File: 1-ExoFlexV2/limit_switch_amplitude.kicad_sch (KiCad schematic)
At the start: 44 parts, among them U21 SN74LVC3G14DCUT_V2, U22 SN74LVC3G14DCUT_V2, U23 SN74LVC3G14DCUT_V2, U24 SN74LVC3G14DCUT_V2, U25 SN74LVC3G14DCUT_V2, U26 SN74LVC3G14DCUT_V2, U27 SN74LVC3G14DCUT_V2, U28 SN74LVC1G32DBVR, U29 SN74LVC1G32DBVR

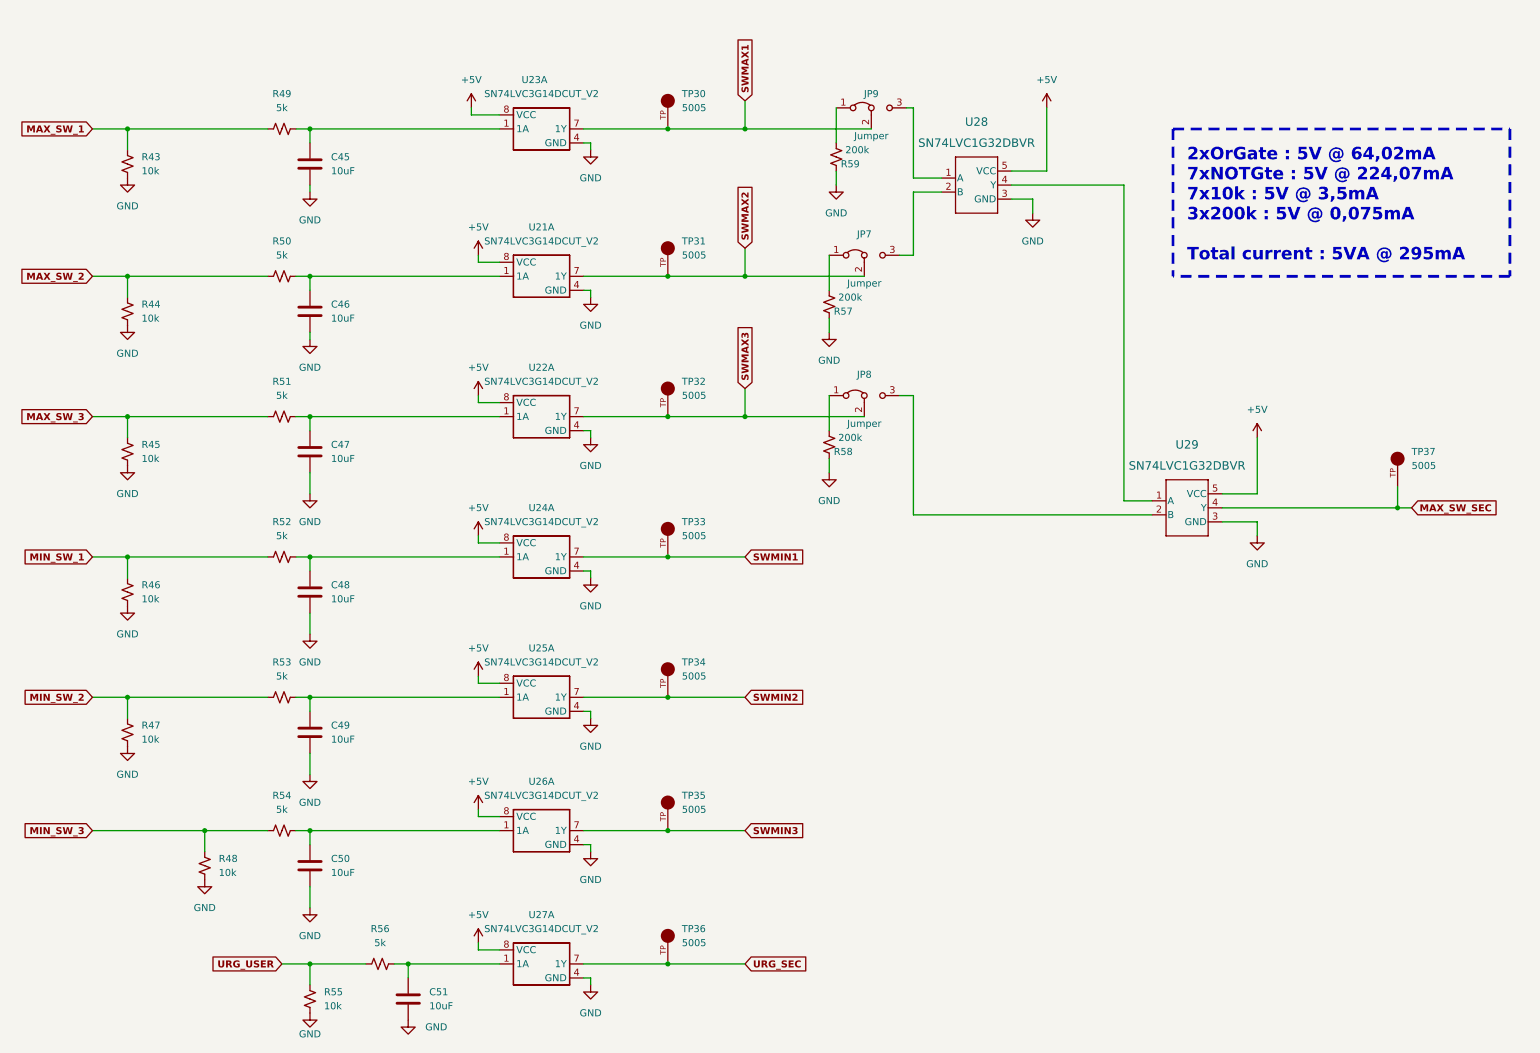
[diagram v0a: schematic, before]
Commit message: Chokes et RC
- Ajout des RF chokes
- Changement des résistance pour 0805
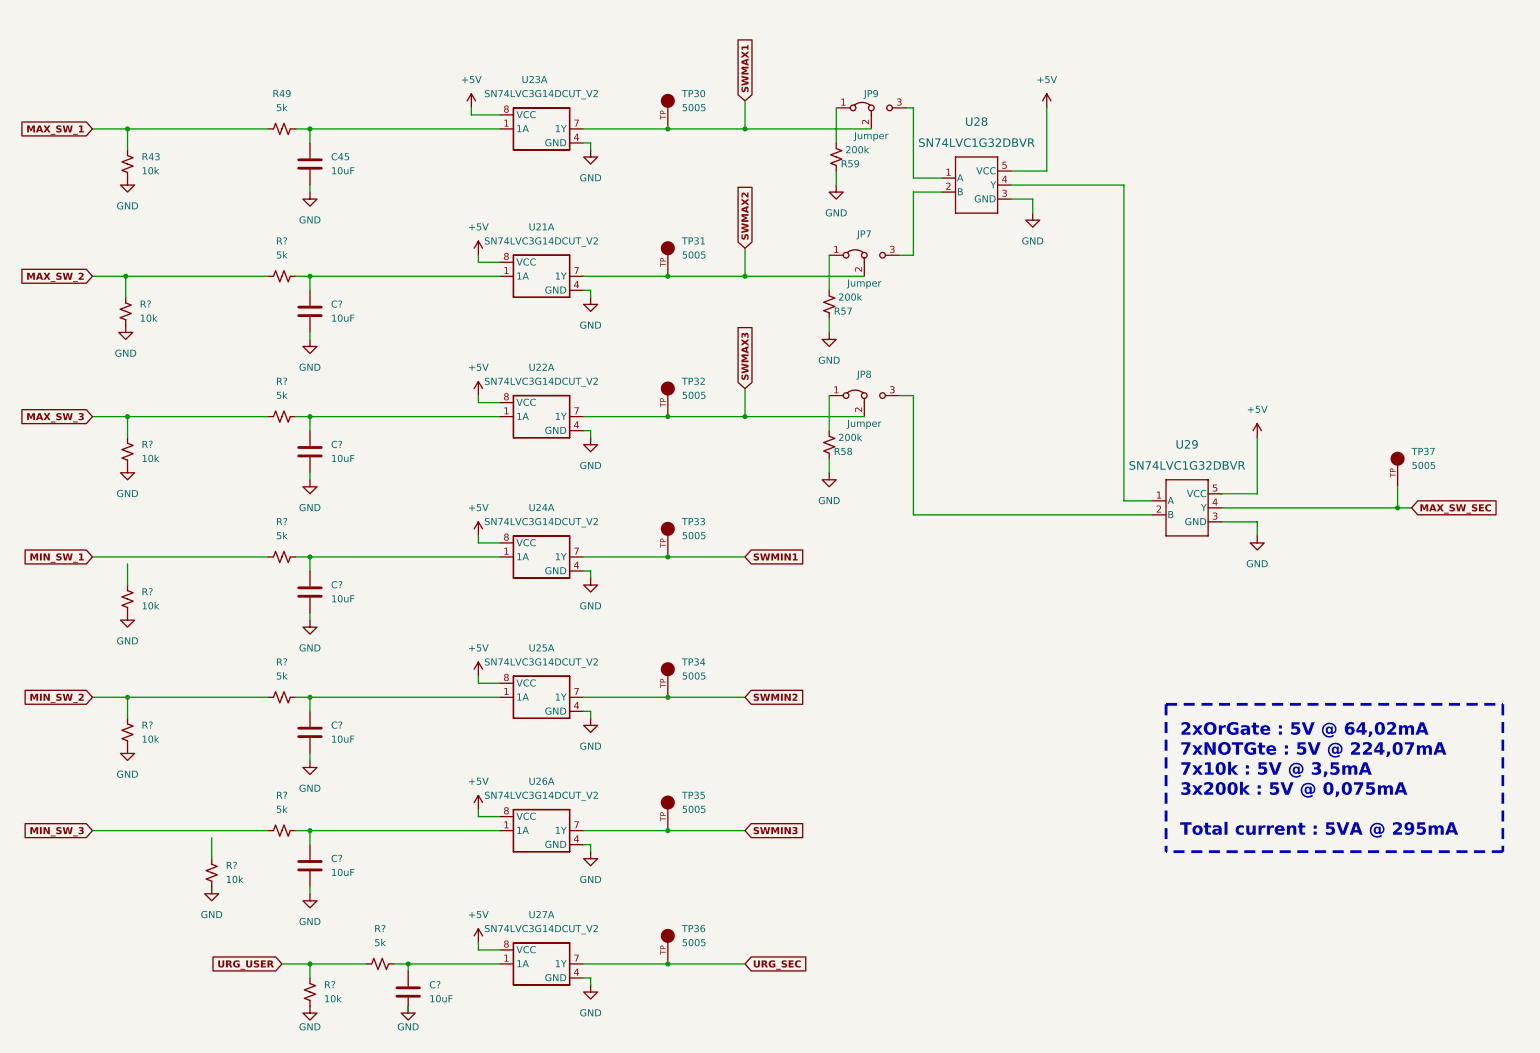
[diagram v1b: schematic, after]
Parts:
- removed C46, C47, C48, C49, C50, C51: 10uF, Capacitor_SMD:C_0603_1608Metric, symbol Device:C
- removed R44, R45, R46, R47, R48, R55: 10k, Resistor_SMD:R_0603_1608Metric, symbol Device:R_Small_US
- removed R50, R51, R52, R53, R54, R56: 5k, Resistor_SMD:R_0603_1608Metric, symbol Device:R_Small_US
- added C? (x6): 10uF, Capacitor_SMD:C_0805_2012Metric, symbol Device:C
- added R? (x6): 5k, Resistor_SMD:R_0805_2012Metric, symbol Device:R_Small_US
- added R? (x6): 10k, Resistor_SMD:R_0805_2012Metric, symbol Device:R_Small_US
- C45: footprint Capacitor_SMD:C_0603_1608Metric -> Capacitor_SMD:C_0805_2012Metric
- R43, R49: footprint Resistor_SMD:R_0603_1608Metric -> Resistor_SMD:R_0805_2012Metric
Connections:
- net GND: now also C?.2, C?.2, C?.2, C?.2, C?.2, C?.2, R?.2, R?.2, R?.2, R?.2, R?.2, R?.2
- net MAX_SW_2: now also R?.1, R?.1
- net MAX_SW_3: now also R?.1, R?.1
- net MIN_SW_1: now also R?.1
- net MIN_SW_2: now also R?.1, R?.1
- net MIN_SW_3: now also R?.1
- net URG_USER: now also R?.1, R?.1
- net at U22.1 (1A): now also C?.1, R?.2
- net at U21.1 (1A): now also C?.1, R?.2
- net at U27.1 (1A): now also C?.1, R?.2
- net at U26.1 (1A): now also C?.1, R?.2
- net at U24.1 (1A): now also C?.1, R?.2
- net at U25.1 (1A): now also C?.1, R?.2

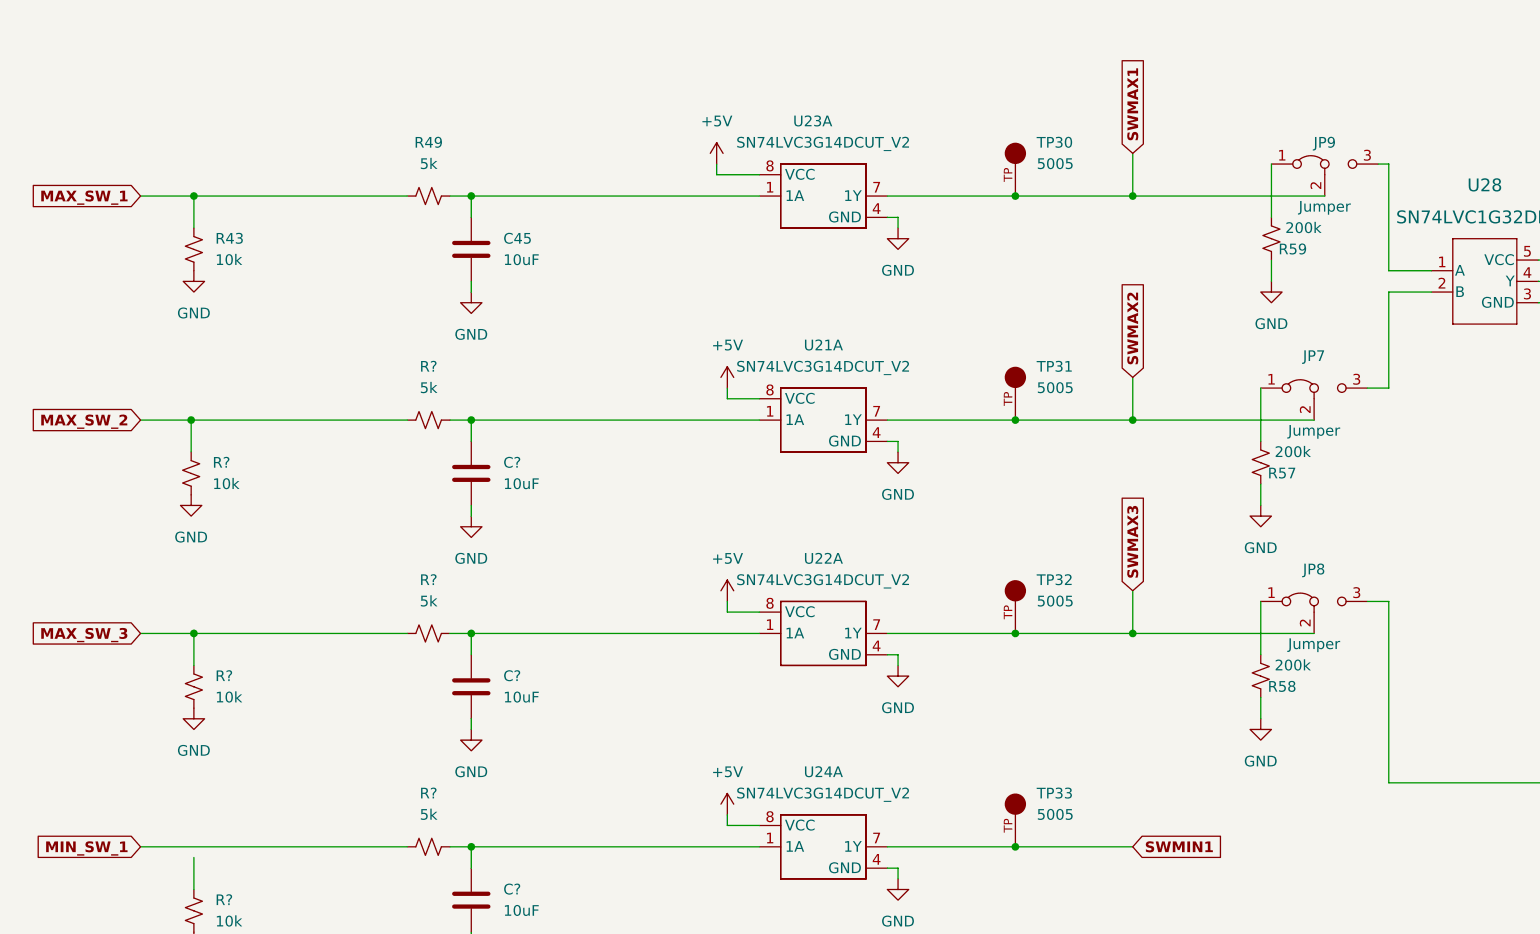
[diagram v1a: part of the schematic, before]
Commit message: Trimmer et jumper
-Changement de symbole de jumper
-Ajout des des trimmer aux endroits nécessaires
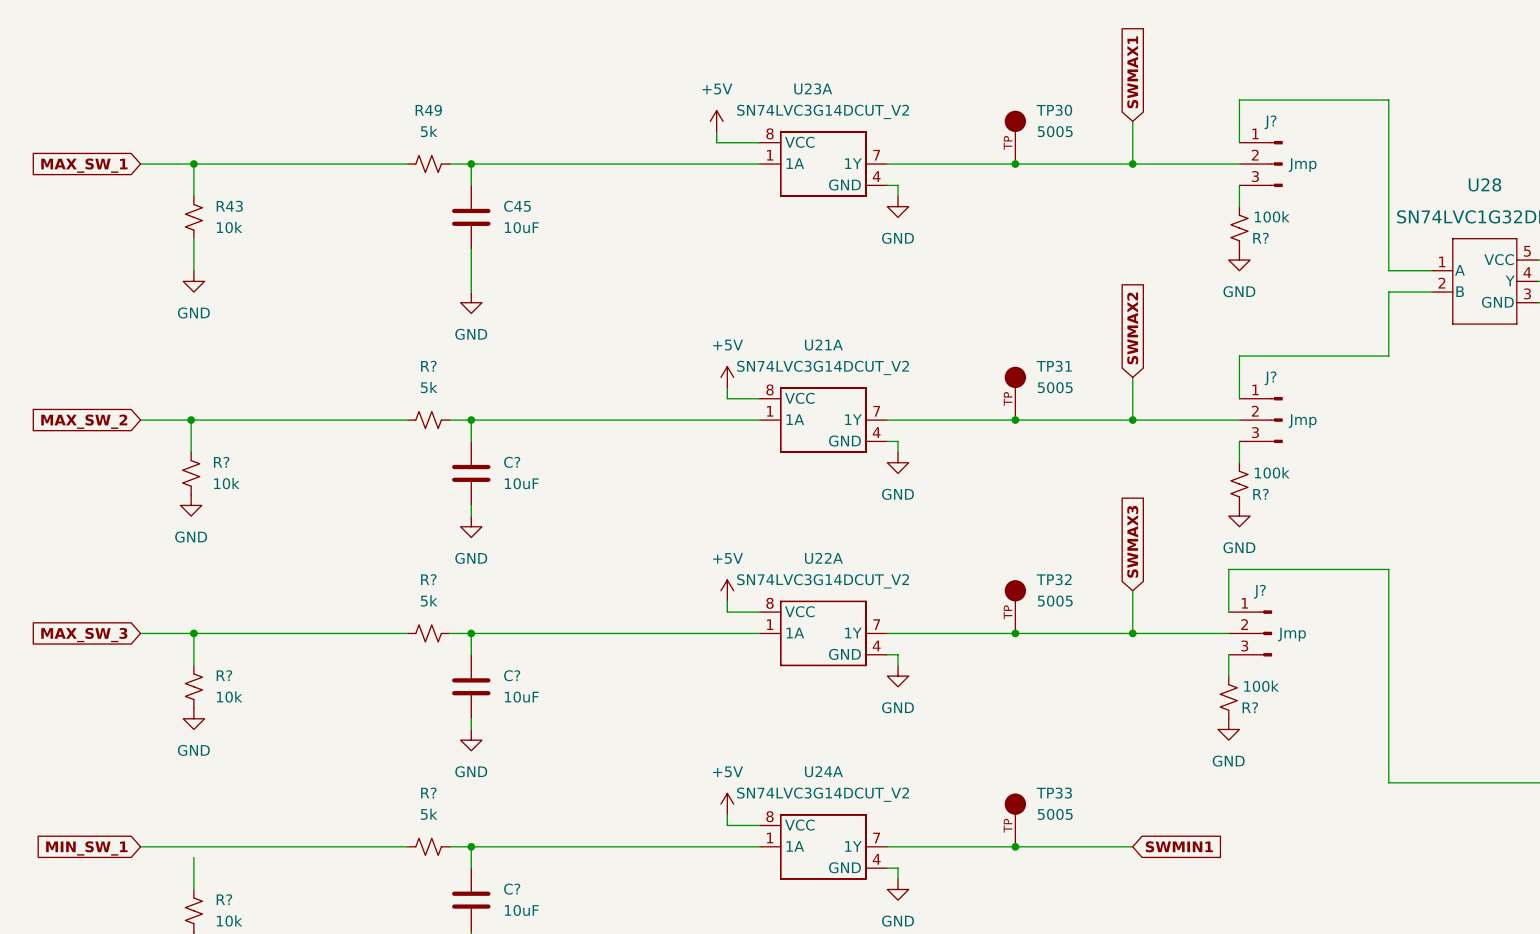
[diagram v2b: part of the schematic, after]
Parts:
- removed JP7, JP8, JP9: Jumper, Connector_PinHeader_2.54mm:PinHeader_1x03_P2.54mm_Vertical, symbol Jumper:Jumper_3_Bridged12
- removed R57, R58, R59: 200k, Resistor_SMD:R_0603_1608Metric, symbol Device:R_Small_US
- added J? (x3): Jmp, symbol Connector:Conn_01x03_Male
- added R? (x3): 100k, Resistor_SMD:R_0805_2012Metric, symbol Device:R_Small_US
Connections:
- net GND: now also R?.2, R?.2, R?.2
- net SWMAX1: now also J?.2 (Pin_2)
- net SWMAX2: now also J?.2 (Pin_2)
- net SWMAX3: now also J?.2 (Pin_2)
- net at U28.2 (B): now also J?.1 (Pin_1)
- net at U29.2 (B): now also J?.1 (Pin_1)
- net at U28.1 (A): now also J?.1 (Pin_1)
- new net: J?.3 (Pin_3), R?.1 (x3)
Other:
- moved on the sheet: C45, R43, R49, TP30, U23A

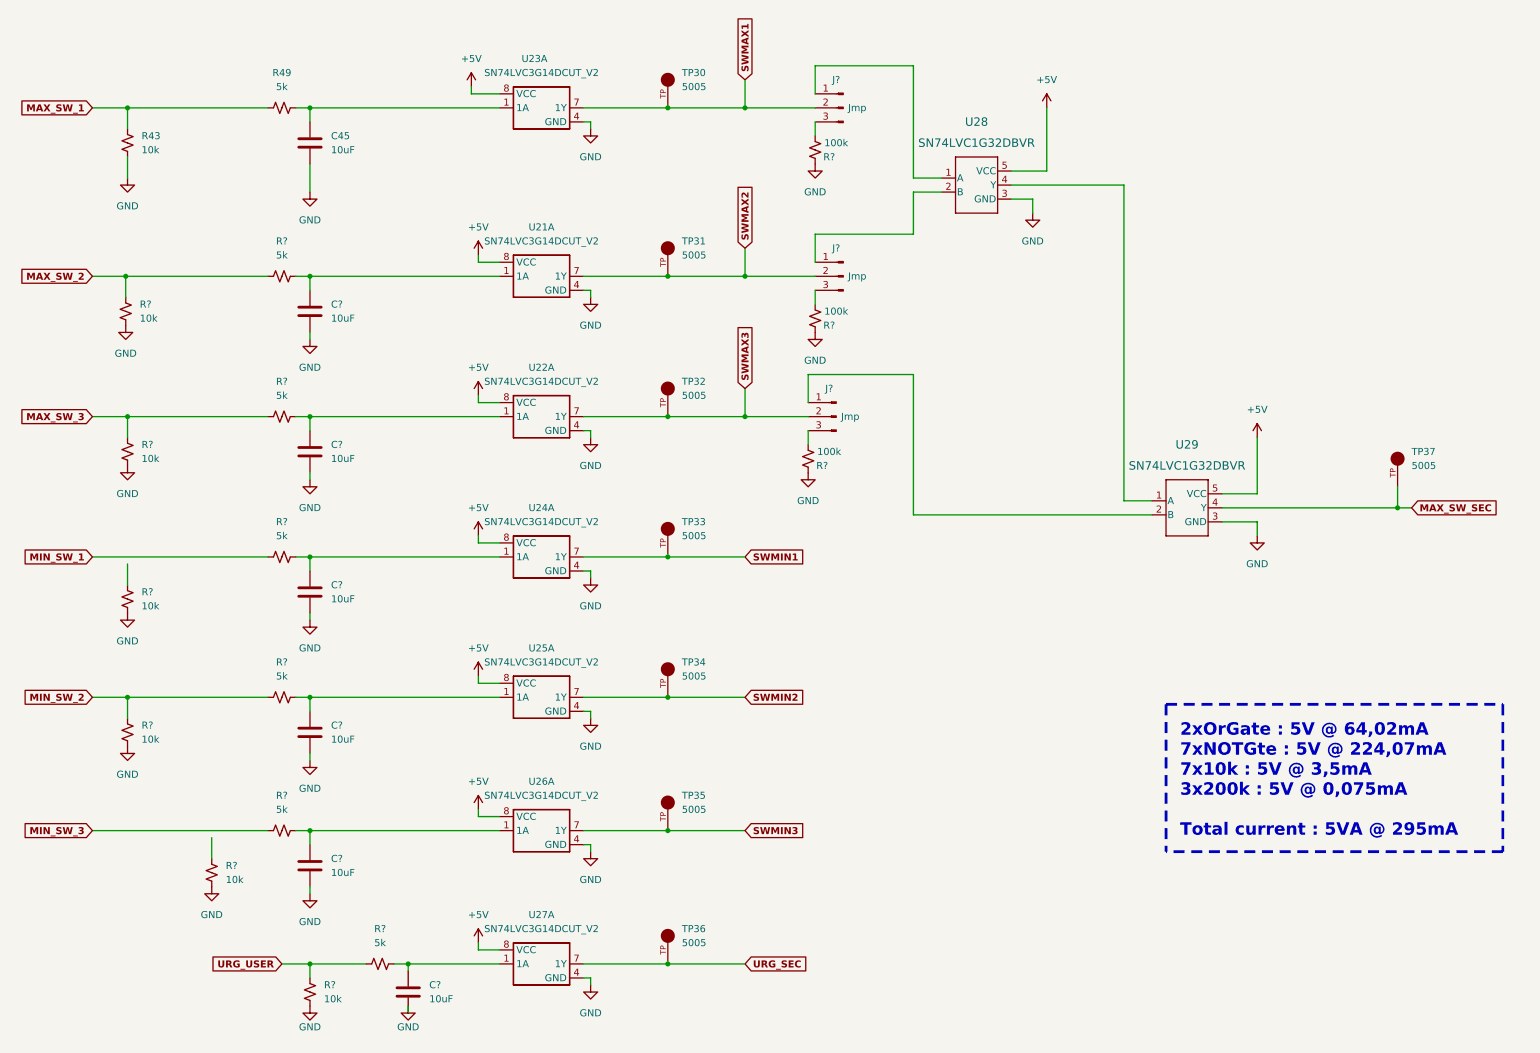
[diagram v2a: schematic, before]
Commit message: Test points et notes
- Ajout de tous les tests point nécessaires
-  Ajoute des sections de notes dans chaque page
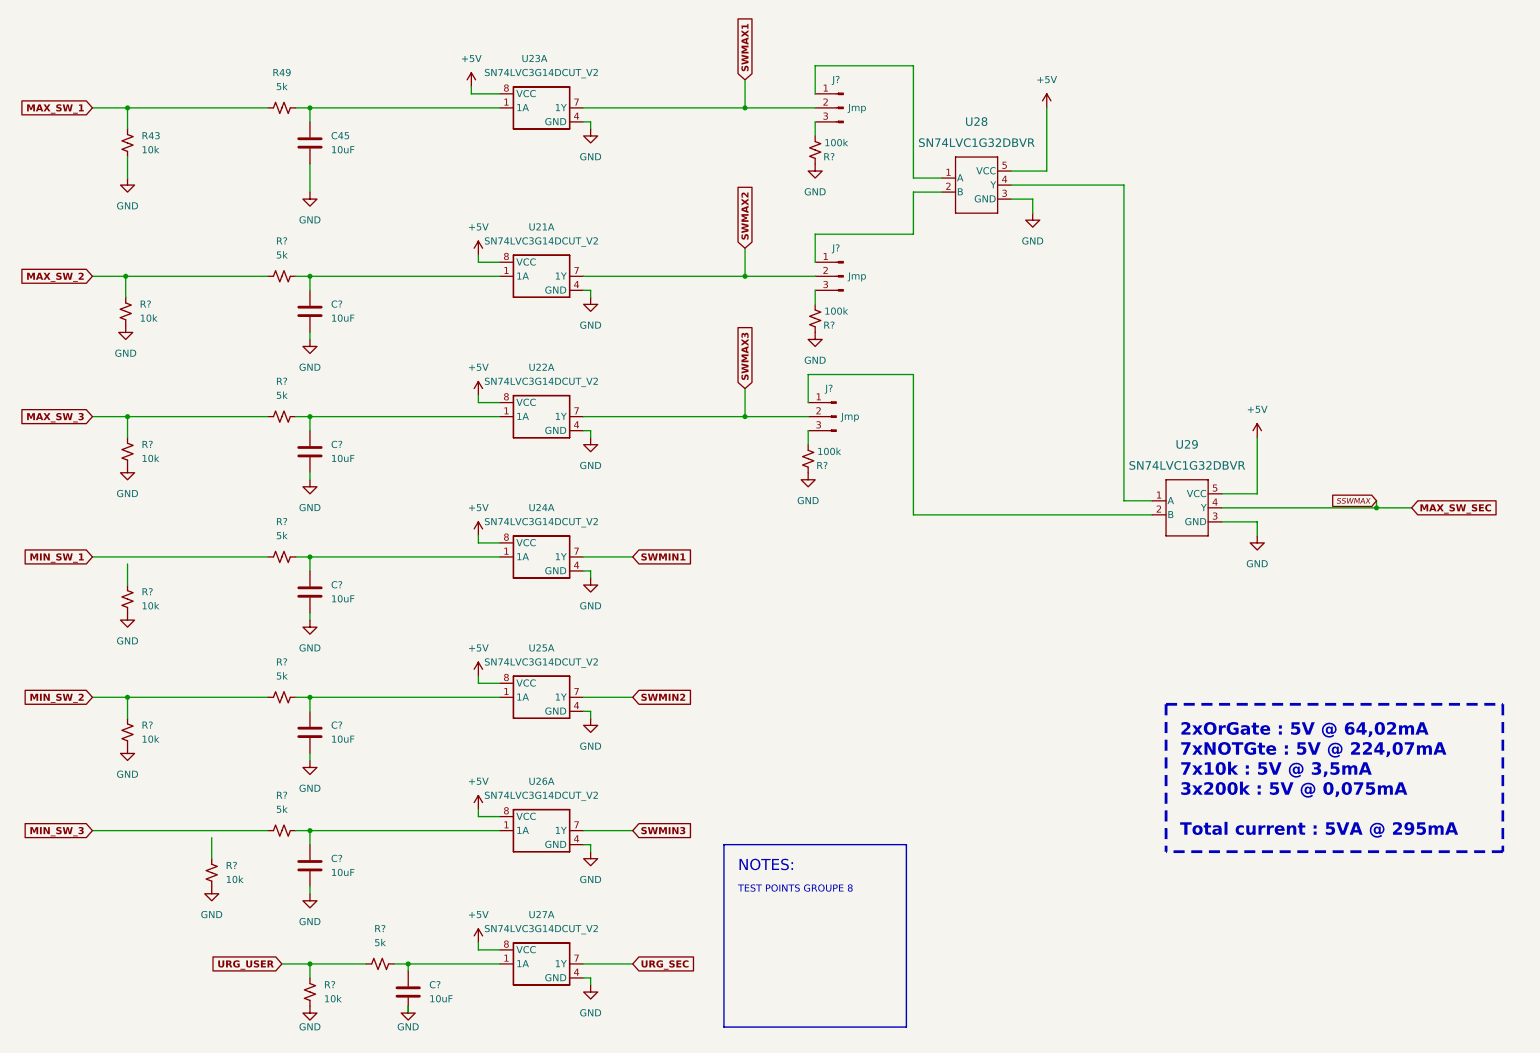
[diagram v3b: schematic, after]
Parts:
- removed TP30, TP31, TP32, TP33, TP34, TP35, TP36, TP37: 5005, FootPrint:KEYSTONE_5005, symbol SymLib:5005
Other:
- note added: "NOTES:"
- note added: "TEST POINTS GROUPE 8"
